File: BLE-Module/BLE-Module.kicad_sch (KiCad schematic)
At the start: 20 parts, among them J1 USB-C

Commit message: Redesigned board
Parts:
- added C_OUT2, ESP32_C_Power1: 22uF, Capacitor_SMD:C_1206_3216Metric, symbol Device:C
- C_OUT1: value 52uF -> 22uF
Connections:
- net GND: now also C_OUT2.2, ESP32_C_Power1.1
- net +V_OUT renamed +3V3
- net +3V3: now also C_OUT2.1, ESP32_C_Power1.2
- net VCC renamed +12V

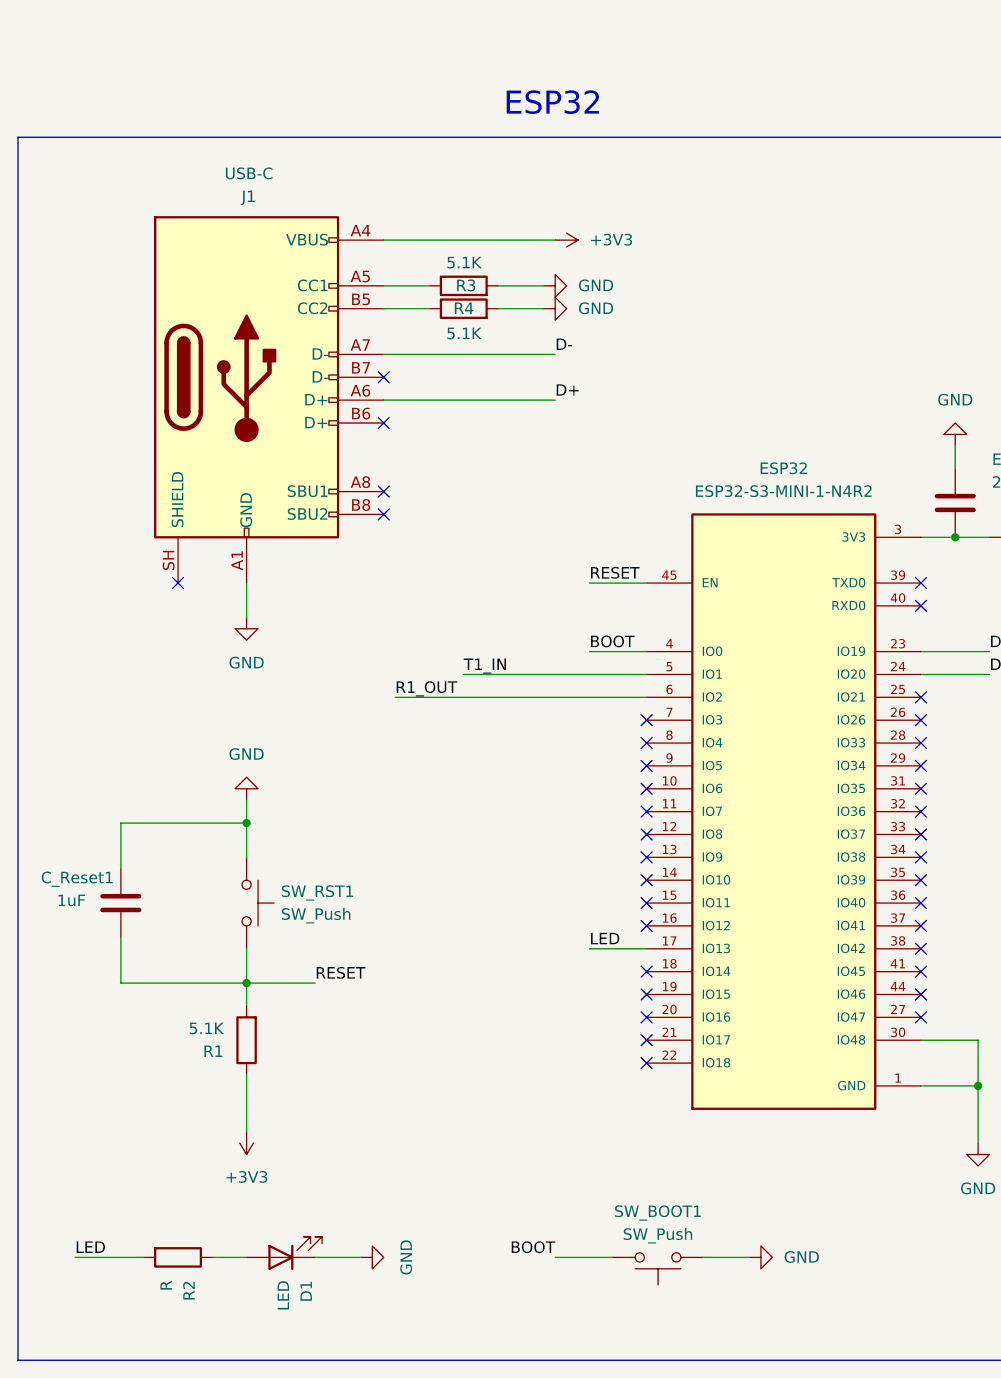
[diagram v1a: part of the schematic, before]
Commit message: Picked USB-C receptacle
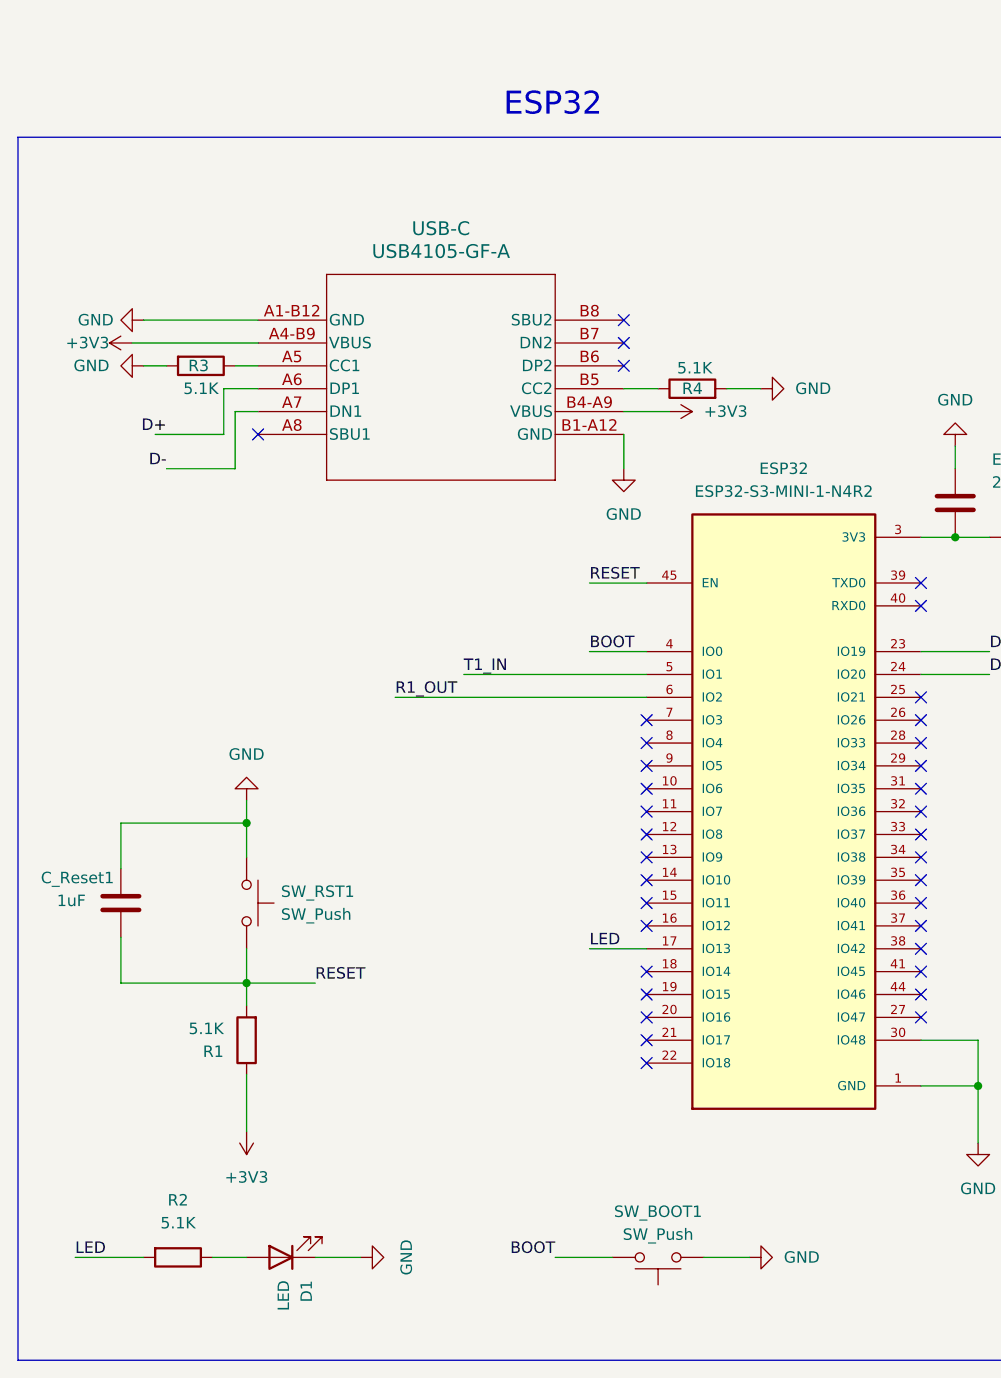
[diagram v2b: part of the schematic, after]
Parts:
- removed J1: USB-C, Connector_USB:USB_C_Receptacle_HRO_TYPE-C-31-M-12, symbol Connector:USB_C_Receptacle_USB2.0_16P
- added USB-C: USB4105-GF-A, USB-C:USB4105_GCT, symbol 2026-04-15_17-12-49:USB4105-GF-A
- BuckConverter1: DKPN (none) -> 945-RPX-4.0-RTR-ND
- ESP32: DKPN (none) -> 1965-ESP32-S3-MINI-1-N4R2TR-ND
- R2: value R -> 5.1K
- UART-SERIAL1: DKPN (none) -> 296-25093-2-ND
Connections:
- net +3V3: now also USB-C.A4-B9 (VBUS), USB-C.B4-A9 (VBUS)
- net D+: now also USB-C.A6 (DP1)
- net D-: now also USB-C.A7 (DN1)
- net GND: now also USB-C.A1-B12 (GND), USB-C.B1-A12 (GND)
- net at R4.1: now also USB-C.B5 (CC2)
- net at R3.1: now also USB-C.A5 (CC1)
- no-connect marks 44 -> 43
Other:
- moved on the sheet: R3, R4

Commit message: Added text and graphics
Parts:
- C1, C2, C3, C4, C_BYPASS1: DKPN (none) -> 399-C0603C104K3RACTUTR-ND
- C_OUT1, C_OUT2, ESP32_C_Power1: DKPN (none) -> 1276-3048-2-ND
- C_Reset1: DKPN (none) -> 1276-1946-2-ND
- R1, R2, R3, R4: DKPN (none) -> RR08P5.1KDTR-ND
- R_FB_1: DKPN (none) -> RR0816P-103-D
- R_FB_2: DKPN (none) -> P4.32KDBTR-ND
- SW_BOOT1, SW_RST1: DKPN (none) -> CKN12218-2-ND
- USB-C1: renamed from USB-C; DKPN (none) -> 2073-USB4105-GF-ATR-ND
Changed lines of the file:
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@@
 			)
 		)
-		(property "Datasheet" ""
+		(property "Datasheet" "https://www.digikey.com/en/products/detail/susumu/RR0816P-512-D/432202?s=N4IgTCBcDaIEpwAwA4AKBWAdARgNIBEAVOAWgDl8QBdAXyA"
 			(at 40.64 137.16 0)
 			(hide yes)
@@
 			)
 		)
-		(property "DKPN" ""
+		(property "DKPN" "RR08P5.1KDTR-ND"
 			(at 40.64 137.16 0)
 			(hide yes)
@@
 			)
 		)
-		(property "Datasheet" ""
+		(property "Datasheet" "https://www.digikey.com/en/products/detail/kemet/C0603C104K3RACTU/416044"
 			(at 246.38 113.03 0)
 			(hide yes)
@@
 			)
 		)
-		(property "DKPN" ""
+		(property "DKPN" "399-C0603C104K3RACTUTR-ND"
 			(at 246.38 113.03 90)
 			(hide yes)
@@
 			)
 		)
-		(property "Datasheet" ""
+		(property "Datasheet" "https://www.digikey.com/en/products/detail/samsung-electro-mechanics/CL31A226KOHNNNE/3888706?s=N4IgTCBcDaIIxgOwDYC0BmADAFgByrFQDkAREAXQF8g"
 			(at 119.38 77.47 0)
 			(hide yes)
@@
 			)
 		)
+		(property "DKPN" "1276-3048-2-ND"
+			(at 119.38 77.47 0)
+			(hide yes)
+			(show_name no)
+			(do_not_autoplace no)
+			(effects
+				(font
+					(size 1.27 1.27)
+				)
+			)
+		)
 		(pin "1"
 		)
@@
 			)
 		)
-		(property "Datasheet" ""
+		(property "Datasheet" "https://www.digikey.com/en/products/detail/susumu/RR0816P-512-D/432202?s=N4IgTCBcDaIEpwAwA4AKBWAdARgNIBEAVOAWgDl8QBdAXyA"
 			(at 90.17 64.77 0)
 			(hide yes)
@@
 			)
 		)
-		(property "DKPN" ""
+		(property "DKPN" "RR08P5.1KDTR-ND"
 			(at 90.17 64.77 90)
 			(hide yes)
@@
 			)
 		)
-		(property "Datasheet" "RPX-4.0-R"
+		(property "Datasheet" "https://www.digikey.com/en/products/detail/recom-power/RPX-4-0-R/14312389"
 			(at 168.91 35.56 0)
 			(hide yes)
@@
 			)
 		)
-		(property "Datasheet" ""
+		(property "Datasheet" "https://www.digikey.com/en/products/detail/samsung-electro-mechanics/CL10B105KP8NNNC/3887604"
 			(at 26.67 121.92 0)
 			(hide yes)
@@
 			)
 		)
-		(property "DKPN" ""
+		(property "DKPN" "1276-1946-2-ND "
 			(at 26.67 121.92 0)
 			(hide yes)
@@
 			)
 		)
-		(property "Datasheet" ""
+		(property "Datasheet" "https://www.digikey.com/en/products/detail/c-k/PTS526SM08SMTR2-LFS/10056623"
 			(at 86.36 166.37 0)
 			(hide yes)
@@
 			)
 		)
-		(property "DKPN" ""
+		(property "DKPN" "CKN12218-2-ND "
 			(at 86.36 161.29 0)
 			(hide yes)
@@
 			)
 		)
-		(property "Datasheet" ""
+		(property "Datasheet" "https://www.digikey.com/en/products/detail/espressif-systems/ESP32-S3-MINI-1-N4R2/22597234"
 			(at 100.33 111.76 0)
 			(hide yes)
@@
 			)
 		)
-		(property "Datasheet" ""
+		(property "Datasheet" "https://www.digikey.com/en/products/detail/kemet/C0603C104K3RACTU/416044"
 			(at 260.35 115.57 0)
 			(hide yes)
@@
 			)
 		)
-		(property "DKPN" ""
+		(property "DKPN" "399-C0603C104K3RACTUTR-ND"
 			(at 260.35 115.57 90)
 			(hide yes)
@@
 			)
 		)
-		(property "Datasheet" ""
+		(property "Datasheet" "https://www.digikey.com/en/products/detail/samsung-electro-mechanics/CL31A226KOHNNNE/3888706?s=N4IgTCBcDaIIxgOwDYC0BmADAFgByrFQDkAREAXQF8g"
 			(at 228.6 82.55 0)
 			(hide yes)
@@
 			)
 		)
-		(property "DKPN" ""
+		(property "DKPN" "1276-3048-2-ND"
 			(at 228.6 82.55 90)
 			(hide yes)
@@
 			)
 		)
-		(property "Datasheet" ""
+		(property "Datasheet" "https://www.digikey.com/en/products/detail/susumu/RR0816P-103-D/432209?s=N4IgTCBcDaIEpwAwA4CMA2ACgWlYgzNgCIgC6AvkA"
 			(at 213.36 60.96 0)
 			(hide yes)
@@
 			)
 		)
-		(property "DKPN" ""
+		(property "DKPN" "RR0816P-103-D"
 			(at 213.36 60.96 0)
 			(hide yes)
@@
 			)
 		)
-		(property "Datasheet" ""
+		(property "Datasheet" "https://www.digikey.com/en/products/detail/kemet/C0603C104K3RACTU/416044"
 			(at 157.48 119.38 0)
 			(hide yes)
@@
 			)
 		)
-		(property "DKPN" ""
+		(property "DKPN" "399-C0603C104K3RACTUTR-ND"
 			(at 157.48 119.38 0)
 			(hide yes)
@@
 			)
 		)
-		(property "Datasheet" ""
+		(property "Datasheet" "https://www.digikey.com/en/products/detail/kemet/C0603C104K3RACTU/416044"
 			(at 246.38 123.19 0)
 			(hide yes)
@@
 			)
 		)
-		(property "DKPN" ""
+		(property "DKPN" "399-C0603C104K3RACTUTR-ND"
 			(at 246.38 123.19 90)
 			(hide yes)
@@
 			)
 		)
-		(property "Datasheet" ""
+		(property "Datasheet" "https://www.digikey.com/en/products/detail/susumu/RR0816P-512-D/432202?s=N4IgTCBcDaIEpwAwA4AKBWAdARgNIBEAVOAWgDl8QBdAXyA"
 			(at 33.02 161.29 0)
 			(hide yes)
@@
 			)
 		)
-		(property "DKPN" ""
+		(property "DKPN" "RR08P5.1KDTR-ND"
 			(at 33.02 161.29 0)
 			(hide yes)
@@
 			)
 		)
-		(property "Datasheet" ""
+		(property "Datasheet" "https://www.digikey.com/en/products/detail/kemet/C0603C104K3RACTU/416044"
 			(at 260.35 125.73 0)
 			(hide yes)
@@
 			)
 		)
-		(property "DKPN" ""
+		(property "DKPN" "399-C0603C104K3RACTUTR-ND"
 			(at 260.35 125.73 90)
 			(hide yes)
@@
 			)
 		)
-		(property "Datasheet" ""
+		(property "Datasheet" "https://www.digikey.com/en/products/detail/susumu/RR0816P-512-D/432202?s=N4IgTCBcDaIEpwAwA4AKBWAdARgNIBEAVOAWgDl8QBdAXyA"
 			(at 35.56 62.23 0)
 			(hide yes)
@@
 			)
 		)
-		(property "DKPN" ""
+		(property "DKPN" "RR08P5.1KDTR-ND"
 			(at 35.56 62.23 90)
 			(hide yes)
@@
 		(dnp no)
 		(fields_autoplaced yes)
-		(property "Reference" "USB-C"
+		(property "Reference" "USB-C1"
 			(at 62.23 46.99 0)
 			(show_name no)
@@
 			)
 		)
-		(property "Datasheet" "USB4105-GF-A"
+		(property "Datasheet" "https://www.digikey.com/en/products/detail/gct/USB4105-GF-A/11198441"
 			(at 41.91 57.15 0)
 			(hide yes)
@@
 			)
 		)
+		(property "DKPN" "2073-USB4105-GF-ATR-ND "
+			(at 41.91 57.15 0)
+			(hide yes)
+			(show_name no)
+			(do_not_autoplace no)
+			(effects
+				(font
+					(size 1.27 1.27)
+				)
+			)
+		)
 		(pin "B7"
 		)
@@
 			(project "BLE-Module"
 				(path "/f32fd4ec-d5e6-44db-8279-3c2039072023"
-					(reference "USB-C")
+					(reference "USB-C1")
 					(unit 1)
 				)
@@
 			)
 		)
-		(property "Datasheet" ""
+		(property "Datasheet" "https://www.digikey.com/en/products/detail/samsung-electro-mechanics/CL31A226KOHNNNE/3888706?s=N4IgTCBcDaIIxgOwDYC0BmADAFgByrFQDkAREAXQF8g"
 			(at 228.6 74.93 0)
 			(hide yes)
@@
 			)
 		)
-		(property "DKPN" ""
+		(property "DKPN" "1276-3048-2-ND"
 			(at 228.6 74.93 90)
 			(hide yes)
@@
 			)
 		)
-		(property "Datasheet" ""
+		(property "Datasheet" "https://www.digikey.com/en/products/detail/c-k/PTS526SM08SMTR2-LFS/10056623"
 			(at 45.72 121.92 0)
 			(hide yes)
@@
 			)
 		)
-		(property "DKPN" ""
+		(property "DKPN" "CKN12218-2-ND "
 			(at 40.64 121.92 90)
 			(hide yes)
@@
 			)
 		)
-		(property "Datasheet" ""
+		(property "Datasheet" "https://www.digikey.com/en/products/detail/panasonic-industry/ERA-3AEB4321V/2026805?s=N4IgTCBcDaIAoBYB0BmMBpAIgIQCoCUBaAOUxAF0BfIA"
 			(at 231.14 50.8 0)
 			(hide yes)
@@
 			)
 		)
-		(property "DKPN" ""
+		(property "DKPN" "P4.32KDBTR-ND"
 			(at 231.14 50.8 90)
 			(hide yes)

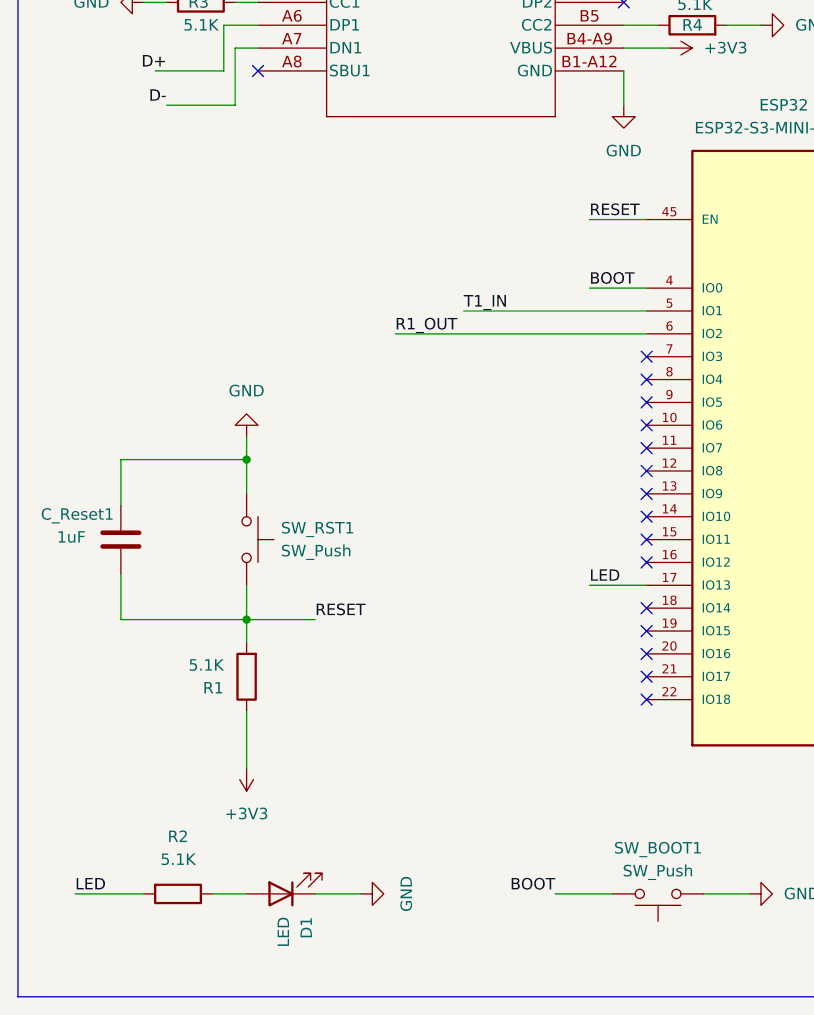
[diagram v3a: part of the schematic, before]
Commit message: Added common-anode LED
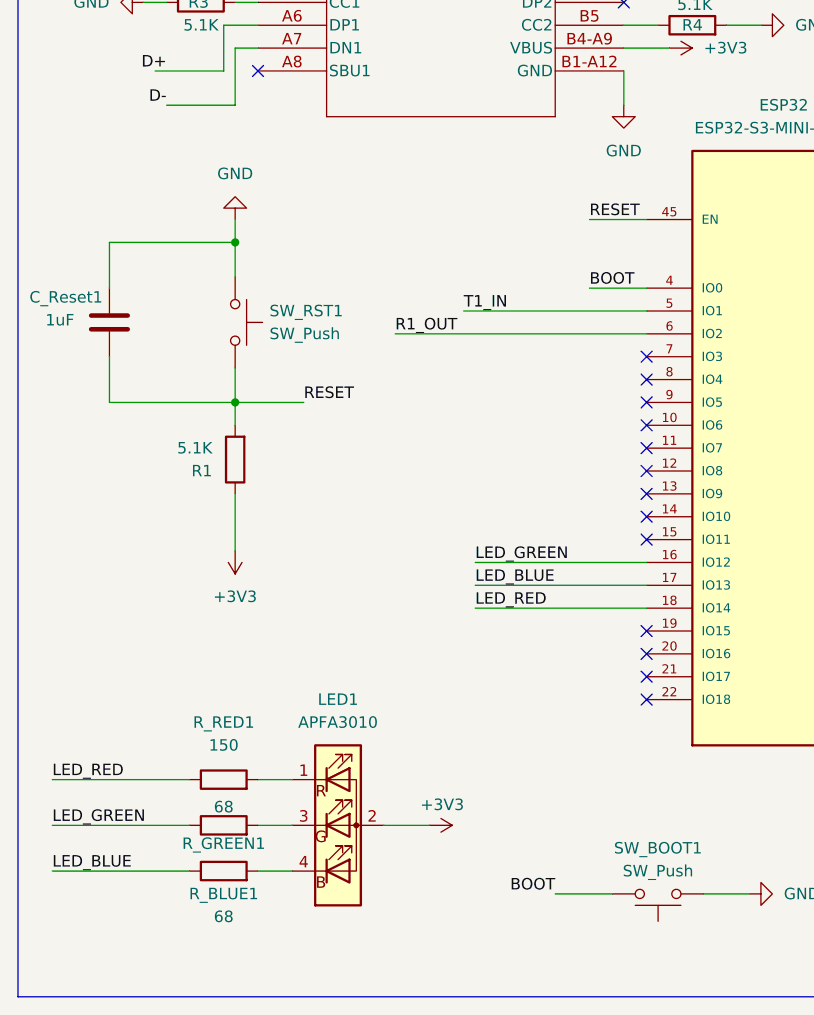
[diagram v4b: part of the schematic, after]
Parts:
- removed D1: LED, LED_SMD:LED_0603_1608Metric, symbol Device:LED
- removed R2: 5.1K, Resistor_SMD:R_0603_1608Metric, symbol Device:R
- added LED1: APFA3010, LED_SMD:LED_Kingbright_APFA3010_3x1.5mm_Horizontal, symbol LED:APFA3010
- added R_BLUE1, R_GREEN1: 68, Resistor_SMD:R_0603_1608Metric, symbol Device:R
- added R_RED1: 150, Resistor_SMD:R_0603_1608Metric, symbol Device:R
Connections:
- net +3V3: now also LED1.2 (A)
- net LED_GREEN: now reaches ESP32.16 (IO12)
- net LED_GREEN: now also R_GREEN1.1
- net LED_RED: now reaches ESP32.18 (IO14)
- net LED_RED: now also R_RED1.1
- net LED renamed LED_BLUE
- net LED_BLUE: now also R_BLUE1.1
- new net: LED1.4 (B), R_BLUE1.2
- new net: LED1.1 (R), R_RED1.2
- new net: LED1.3 (G), R_GREEN1.2
- no-connect marks 43 -> 41
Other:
- moved on the sheet: C_Reset1, R1, SW_RST1

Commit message: updated docs
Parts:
- added +12V1: +12V, TestPoint:TestPoint_THTPad_2.5x2.5mm_Drill1.2mm, symbol Connector:TestPoint
- added 12_PIN1: FTSH-106-01-L-DV, FTSH-106-01-L-DV:SAMTEC_FTSH-106-01-L-DV, symbol FTSH-106-01-L-DV:FTSH-106-01-L-DV
- added GND1: GND, TestPoint:TestPoint_THTPad_2.5x2.5mm_Drill1.2mm, symbol Connector:TestPoint
- added RX1: TX_OUT, TestPoint:TestPoint_THTPad_2.5x2.5mm_Drill1.2mm, symbol Connector:TestPoint
- added TX1: RX_IN, TestPoint:TestPoint_THTPad_2.5x2.5mm_Drill1.2mm, symbol Connector:TestPoint
- R_BLUE1, R_GREEN1: value 68 -> 120; DKPN RR08Q68DTR-ND -> P120DBTR-ND
- R_RED1: value 150 -> 120; DKPN P150DBTR-ND -> P120DBTR-ND
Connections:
- net +12V: now also +12V1.1
- net GND: now also GND1.1
- net RX_IN: now also TX1.1
- net TX_OUT: now also RX1.1

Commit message: Saving before I change the power plane
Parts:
- 12_PIN1: footprint FTSH-106-01-L-DV:SAMTEC_FTSH-106-01-L-DV -> 12_PIN:SAMTEC_FTSH-106-01-L-DV
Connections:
- net +12V: now also 12_PIN1.11
- net +3V3: now also 12_PIN1.12
- net GND: now also 12_PIN1.01, 12_PIN1.02
- net CS: now reaches 12_PIN1.03
- net CS: now also ESP32.34 (IO38)
- net IO_4: now reaches 12_PIN1.04
- net IO_4: now also ESP32.38 (IO42)
- net MISO: now reaches 12_PIN1.05
- net MISO: now also ESP32.33 (IO37)
- net IO_3: now reaches 12_PIN1.06
- net IO_3: now also ESP32.37 (IO41)
- net MOSI: now reaches 12_PIN1.07
- net MOSI: now also ESP32.31 (IO35)
- net IO_2: now reaches 12_PIN1.08
- net IO_2: now also ESP32.36 (IO40)
- net SCK: now reaches 12_PIN1.09
- net SCK: now also ESP32.32 (IO36)
- net IO_1: now reaches 12_PIN1.10
- net IO_1: now also ESP32.35 (IO39)
- no-connect marks 41 -> 33

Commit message: Changed design to 4-layer
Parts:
- added C8: 10uF, Capacitor_SMD:C_1210_3225Metric, symbol Device:C
- renumbered C_Reset1 to C10, C_BYPASS1 to C5, C_OUT1 to C6, C_OUT2 to C7, ESP32_C_Power1 to C9, R_FB_2 to R2, R_FB_1 to R5, R_RED1 to R6, R_GREEN1 to R7, R_BLUE1 to R8
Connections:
- net +12V: now also C8.1
- net +3V3: no longer USB-C1.A4-B9 (VBUS), USB-C1.B4-A9 (VBUS)
- net GND: now also C8.2
- net PG: no longer names the net of BuckConverter1.13 (PGS)
- no-connect marks 33 -> 36
